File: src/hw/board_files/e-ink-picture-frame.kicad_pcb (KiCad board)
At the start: 4 copper layers, 177 x 118 mm, 106 parts, among them J1 USB_C_Receptacle_USB2.0_16P, J2 Conn_01x03, J3 Molex 104031-0811, J4 Conn_01x10, Q1 AO3401A, Q2 BSS138, Q3 Si1308EDL, Q4 SI2301CDS-T1-E3, SW1 SW_Push, SW2 SW_Push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

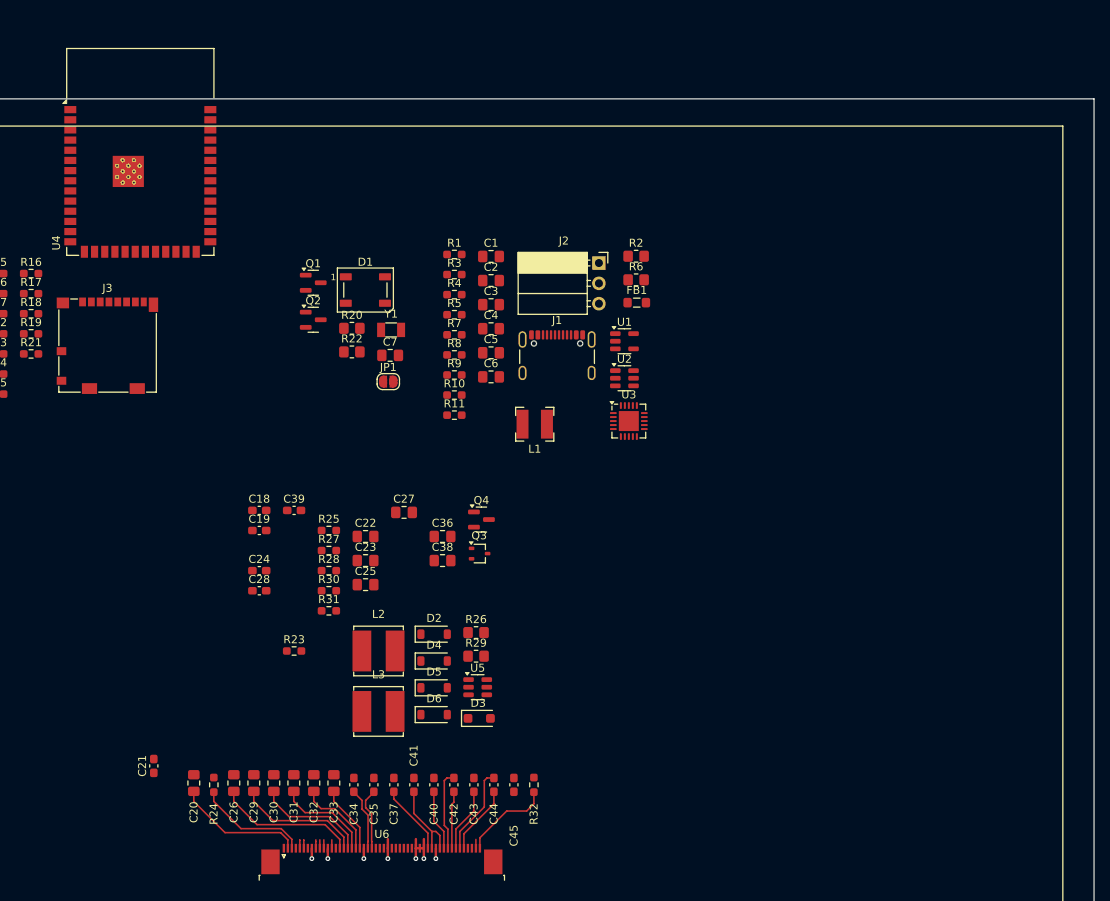
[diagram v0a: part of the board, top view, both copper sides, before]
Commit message: Started display circuit layout
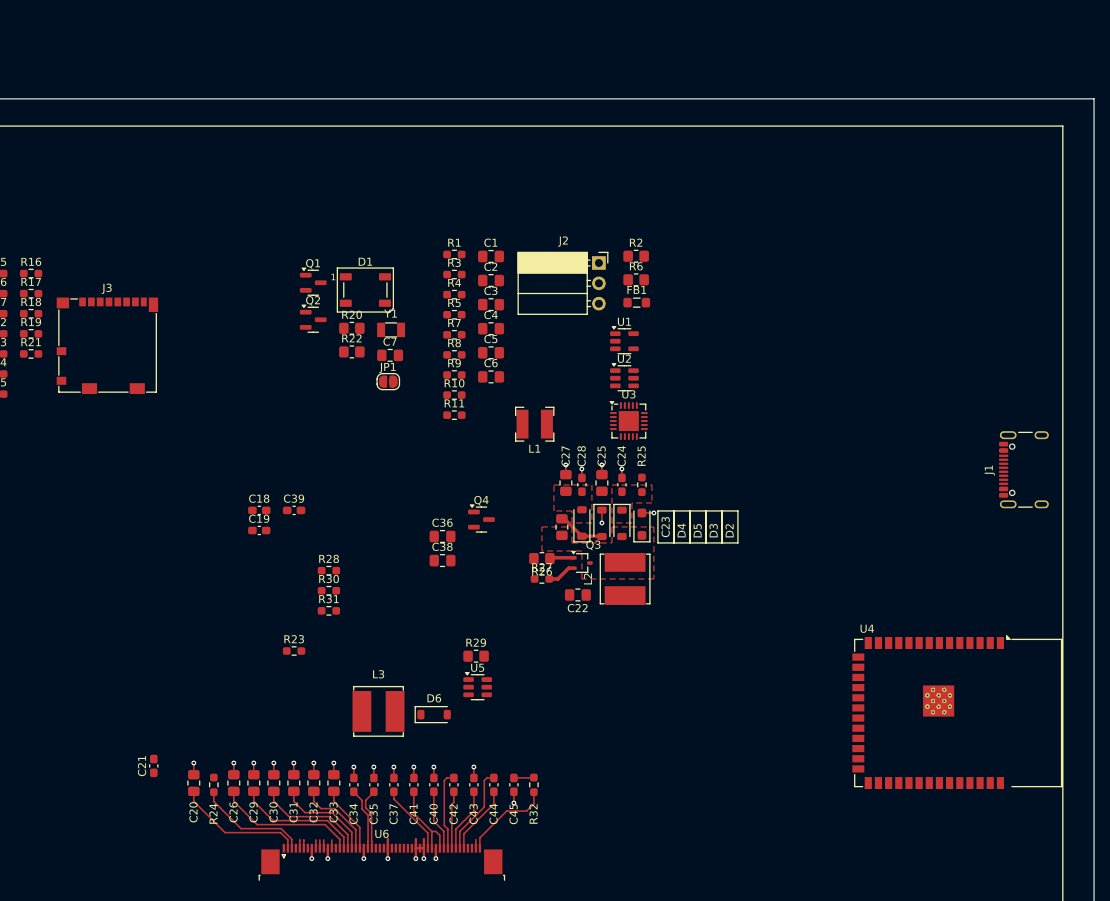
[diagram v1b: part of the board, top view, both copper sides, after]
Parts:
- moved U4 124.0 mm to (212.0, 117.8), turned to -90 degrees
- moved J1 60.9 mm to (221.4, 87.3), turned to 90 degrees
- moved C24 46.6 mm to (170.0, 89.2), turned to 90 degrees
- moved C28 42.4 mm to (165.0, 89.2), turned to 90 degrees
- moved R25 39.5 mm to (172.5, 89.2), turned to 90 degrees
- moved C25 32.2 mm to (167.5, 89.0), turned to 90 degrees
- moved L2 32.1 mm to (170.4, 101.0), turned to 90 degrees
- moved D3 31.7 mm to (172.5, 94.2), turned to 90 degrees
- moved D5 29.4 mm to (167.5, 94.0), turned to -90 degrees
- moved C22 27.5 mm to (164.5, 103.0), turned to 180 degrees
- moved D2 27.3 mm to (170.0, 94.0), turned to -90 degrees
- moved R27 26.9 mm to (160.0, 101.0)
- moved D4 25.3 mm to (165.0, 94.0), turned to 90 degrees
- moved C23 24.9 mm to (162.5, 94.5), turned to 90 degrees
- moved C27 20.6 mm to (163.0, 89.0), turned to 90 degrees
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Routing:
- net GND: track 13.5 -> 41.1 mm, vias 7 -> 27
- net Net-(D4-K): track 0.00 -> 5.92 mm
- net /Display/RESEH: track 1.05 -> 4.69 mm
- net /Display/GDRH: track 1.05 -> 4.09 mm
- net Net-(C45-Pad1): track 0.00 -> 2.52 mm
- added copper zone on F.Cu, net /Display/VGL
- added copper zone on F.Cu, net /Display/VPH
- added copper zone on F.Cu, net Net-(D2-A)

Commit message: Laid out main components
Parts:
- added H1: MountingHole_Pad, MountingHole:MountingHole_3.2mm_M3_Pad, F.Cu at (57.0, 46.0)
- added H2: MountingHole_Pad, MountingHole:MountingHole_3.2mm_M3_Pad, F.Cu at (224.0, 46.0)
- added H3: MountingHole_Pad, MountingHole:MountingHole_3.2mm_M3_Pad, F.Cu at (224.0, 154.0)
- added H4: MountingHole_Pad, MountingHole:MountingHole_3.2mm_M3_Pad, F.Cu at (57.0, 154.0)
- J3: footprint Connector_Card:microSD_HC_Molex_104031-0811 -> Connector_Card:microSD_HC_Hirose_DM3D-SF
- moved J1 173.8 mm to (55.6, 139.3), turned to -90 degrees
- moved SW1 164.0 mm to (218.8, 72.8)
- moved SW2 164.0 mm to (218.8, 97.8)
- moved SW3 164.0 mm to (218.8, 122.8)
- moved U4 147.3 mm to (65.0, 108.5), turned to 90 degrees
- moved C13 136.8 mm to (215.0, 125.0), turned to 90 degrees
- moved FB1 132.7 mm to (64.3, 144.2)
- moved C12 130.4 mm to (215.0, 100.0), turned to 90 degrees
- moved J2 129.0 mm to (71.7, 148.3), turned to 90 degrees
- moved C9 127.9 mm to (215.0, 75.0), turned to 90 degrees
- moved U2 123.5 mm to (64.3, 139.3)
- moved R4 114.4 mm to (64.3, 142.2)
- moved R2 112.7 mm to (100.0, 147.5), turned to 180 degrees
- moved D1 112.2 mm to (222.0, 139.2)
- moved R1 111.7 mm to (69.1, 138.3)
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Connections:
- U4 pad 23: unconnected-(U4-IO21-Pad23) -> /Microcontroller/BAT_~{PG}
- U4 pad 24: unconnected-(U4-IO47-Pad24) -> /Microcontroller/BAT_STAT1
- U4 pad 25: unconnected-(U4-IO48-Pad25) -> /Microcontroller/BAT_STAT2
- U4 pad 29: /Microcontroller/BAT_~{PG} -> unconnected-(U4-IO36-Pad29)
- U4 pad 30: /Microcontroller/BAT_STAT1 -> unconnected-(U4-IO37-Pad30)
- U4 pad 31: /Microcontroller/BAT_STAT2 -> unconnected-(U4-IO38-Pad31)
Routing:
- net /Microcontroller/SPI_MOSI: track 0.00 -> 151.7 mm, vias 0 -> 2
- net /Microcontroller/SPI_SCK: track 0.00 -> 144.7 mm, vias 0 -> 2
- net /Microcontroller/SD_CS: track 0.00 -> 79.0 mm, vias 0 -> 2
- net /Microcontroller/SPI_MISO: track 0.00 -> 72.4 mm, vias 0 -> 2
- net GND: track 41.1 -> 97.7 mm, vias 27 -> 59
- net VBUS: track 0.00 -> 53.0 mm, vias 0 -> 4
- net /Microcontroller/GPIO40: track 0.00 -> 35.4 mm
- net /Microcontroller/GPIO41: track 0.00 -> 32.6 mm
- net +3V3: track 0.00 -> 30.9 mm, vias 0 -> 17
- net /Display/GDRC: track 1.05 -> 31.5 mm, vias 0 -> 2
- net /Microcontroller/GPIO42: track 0.00 -> 29.7 mm
- net /Microcontroller/USB_D+: track 0.00 -> 27.3 mm
- net /Microcontroller/USB_D-: track 0.00 -> 27.2 mm
- net /Display/GDRH: track 4.09 -> 28.5 mm, vias 0 -> 2
- net /Display/RESEH: track 4.69 -> 26.6 mm, vias 0 -> 2
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- added copper zone on F.Cu, net +3V3
- added copper zone on In2.Cu, net +3V3
- added copper zone on F.Cu, net +3V3_EPD
- added copper zone on F.Cu, net /Display/GDRC
- added copper zone on F.Cu, net /Display/VPC
- added copper zone on F.Cu, net Net-(D6-K)
- added copper zone on F.Cu, net Net-(U1-SW)
- added copper zone on F.Cu, net VBAT
- added copper zone on F.Cu, net V_SYS
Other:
- outline, holes or cut-outs redrawn
- board text added: "0"
- board text added: "1"
- board text added: "BS0"
